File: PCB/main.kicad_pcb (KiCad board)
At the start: 2 copper layers, 135.6 x 65.7 mm, 103 parts, among them K1 HK19F-DCxxV-SHC, Q1 BC337, Q10 BC817, Q11 BC817, Q12 TPCA8120,L1Q, Q13 BC817, Q14 BC817, Q15 BC817, Q16 TPCA8120,L1Q, Q17 BC817, Q18 TPCA8120,L1Q, Q2 BC817, Q3 TPCA8120,L1Q, Q4 BC817, Q5 TPCA8120,L1Q, Q6 TPCA8120,L1Q, Q7 TPCA8120,L1Q, Q8 BC817, Q9 BC817, SW1 config, U1 ESP32-S2-DevKitM, U2 L7805

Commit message: First release for a single (66mm * 118mm) PCB ;-)
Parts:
- removed Q1: BC337, Package_TO_SOT_THT:TO-92_Inline_Wide
- added Q19: BC817, Package_TO_SOT_SMD:SOT-23, F.Cu at (120.2, 68.2)
- Q10, Q11, Q13, Q14, Q15, Q4, Q8, Q9, R11, R12, R3, R4, RA14, RA15, RA16, RA17, RA20, RA22, RA23, RA24, RA25, RA27, RA28, RA30, RA31, RA32, RA33, RA34, RA35, RA36: moved to B.Cu
- RA18, RA19: value 120 -> 33K; moved to B.Cu
- moved SW1 208.7 mm to (129.2, 109.5), turned to -90 degrees
- moved RA3 207.8 mm to (148.9, 103.4)
- moved RA4 207.6 mm to (148.8, 106.0)
- moved RA5 207.5 mm to (148.8, 108.5)
- moved RA7 207.3 mm to (148.9, 94.3)
- moved RA8 207.2 mm to (148.8, 97.5)
- moved RA6 207.2 mm to (148.9, 100.0)
- moved Q4 202.2 mm to (148.2, 70.8), turned to 180 degrees
- moved RV1 197.9 mm to (120.1, 110.6), turned to 90 degrees
- moved R5 197.4 mm to (124.0, 66.7), turned to 90 degrees
- moved R1 195.3 mm to (120.0, 64.5), turned to 180 degrees
- moved RV2 192.2 mm to (114.5, 115.7), turned to -90 degrees
- moved R2 191.8 mm to (116.2, 68.7), turned to -90 degrees
- moved RA14 185.8 mm to (132.6, 80.1), turned to 90 degrees
- moved RA16 185.7 mm to (133.0, 94.4), turned to -90 degrees
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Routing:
- net GND: track 0.00 -> 461.9 mm, vias 0 -> 9
- net +12V: track 0.00 -> 233.5 mm, vias 0 -> 8
- net tempPower: track 0.00 -> 185.0 mm, vias 0 -> 2
- net 5V: track 0.00 -> 169.7 mm, vias 0 -> 5
- net c_rearLight: track 0.00 -> 145.7 mm, vias 0 -> 1
- net i_bykeStand: track 0.00 -> 128.3 mm, vias 0 -> 1
- net Net-(D1-A): track 0.00 -> 85.9 mm, vias 0 -> 1
- net i_startButton: track 0.00 -> 85.8 mm, vias 0 -> 1
- net Net-(Q10-C): track 0.00 -> 84.5 mm, vias 0 -> 3
- net Net-(Q6-G): track 0.00 -> 84.1 mm, vias 0 -> 1
- net Net-(Q12-G): track 0.00 -> 83.6 mm, vias 0 -> 3
- net c_rightArrow: track 0.00 -> 80.9 mm, vias 0 -> 3
- net i_upLight: track 0.00 -> 71.4 mm
- net c_engineOFF: track 0.00 -> 71.3 mm, vias 0 -> 1
- net i_downLight: track 0.00 -> 67.9 mm
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- added copper zone on B.Cu, net GND
- added copper zone on F.Cu, net GND
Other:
- board size 135.6 x 65.7 mm -> 117.9 x 65.7 mm

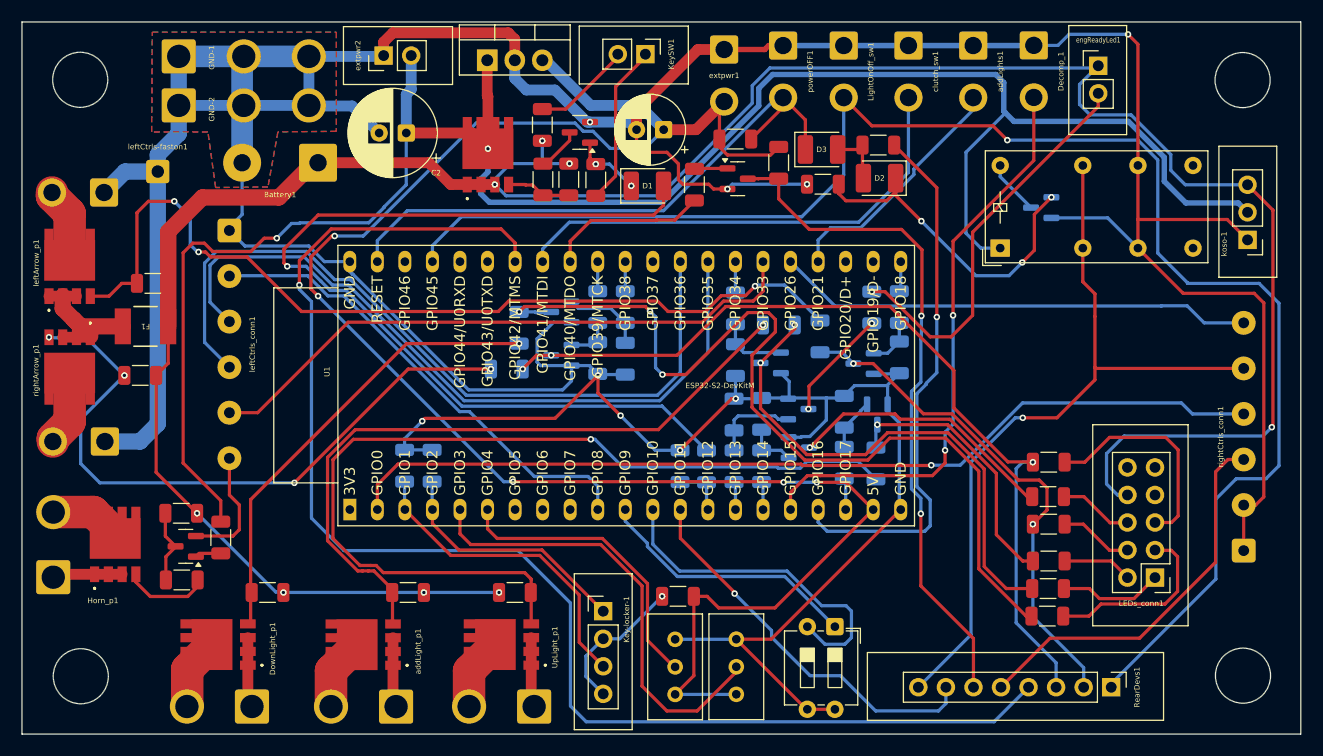
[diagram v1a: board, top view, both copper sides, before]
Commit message: Fixes and size reductuion
- Mosfets' power lines have been added
- 1.5 mm size reduction
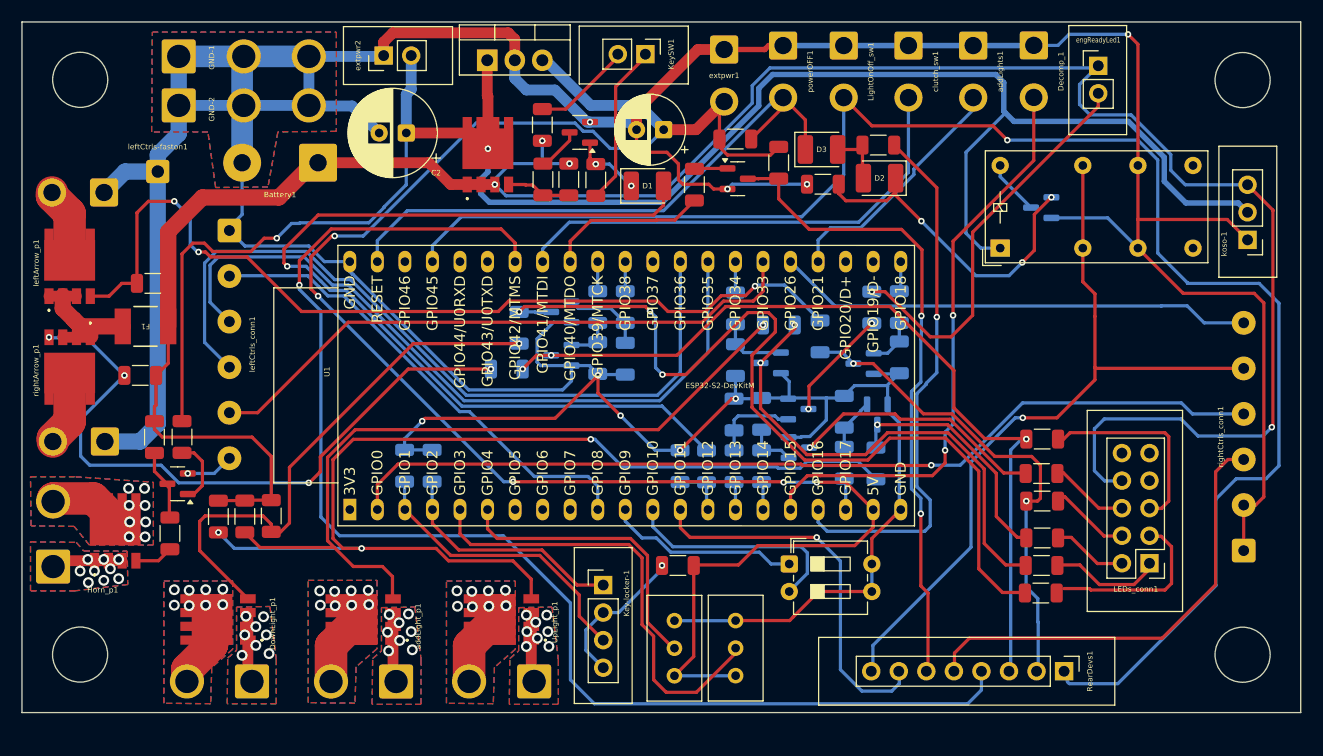
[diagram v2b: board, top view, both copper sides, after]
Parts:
- moved RA10 28.2 mm to (72.3, 99.3), turned to -90 degrees
- moved RA9 16.6 mm to (74.8, 99.3), turned to -90 degrees
- moved RA29 9.93 mm to (69.0, 92.0)
- moved RA21 7.44 mm to (66.4, 92.0), turned to 90 degrees
- moved SW1 7.15 mm to (125.0, 103.7), turned to 0 degrees
- moved RA11 7.06 mm to (77.2, 99.3), turned to -90 degrees
- moved Q17 5.82 mm to (68.6, 96.3)
- moved RearDevs1 4.59 mm to (150.3, 113.6)
- moved RA26 4.43 mm to (67.9, 100.9), turned to 90 degrees
- moved R6 2.84 mm to (114.7, 103.8)
- moved Key-locker-1 2.41 mm to (107.8, 105.6)
- moved DownLight_p1 2.31 mm to (75.4, 114.5)
- moved Q5 2.31 mm to (85.7, 108.8)
- moved Q6 2.31 mm to (98.4, 108.8)
- moved Q7 2.31 mm to (72.3, 108.8)
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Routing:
- net +12V: track 233.5 -> 217.8 mm, vias 8 -> 4
- net Net-(Q6-G): track 84.1 -> 95.6 mm, vias 1 -> 3
- net tempPower: track 185.0 -> 174.4 mm
- net Net-(U1-GPIO10/TOUCH10/ADC1_CH9/FSPICS0/FSPIIO4): track 31.5 -> 21.1 mm
- net GND: track 461.9 -> 452.3 mm
- net Net-(Q7-G): track 42.3 -> 49.9 mm
- net Net-(Q5-G): track 63.9 -> 71.2 mm
- net c_horn: track 11.2 -> 4.42 mm, vias 0 -> 1
- net Net-(U1-GPIO9/TOUCH9/ADC1_CH8/FSPIHD): track 24.6 -> 17.8 mm
- net i_bykeStand: track 128.3 -> 122.3 mm
- net c_brakeSwitch: track 36.0 -> 41.9 mm
- net c_rearLight: track 145.7 -> 150.9 mm
- net Net-(Q18-G): track 7.95 -> 3.57 mm
- net Net-(Q17-B): track 2.41 -> 6.11 mm
- net c_startEngine: track 63.0 -> 59.8 mm
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- added copper zone on B.Cu, net Net-(DownLight_p1-Pin_1)
- added copper zone on F.Cu, net Net-(DownLight_p1-Pin_1)
- added copper zone on B.Cu, net Net-(DownLight_p1-Pin_2)
- added copper zone on F.Cu, net Net-(DownLight_p1-Pin_2)
- added copper zone on B.Cu, net Net-(Horn_p1-Pin_1)
- added copper zone on F.Cu, net Net-(Horn_p1-Pin_1)
- added copper zone on B.Cu, net Net-(Horn_p1-Pin_2)
- added copper zone on F.Cu, net Net-(Horn_p1-Pin_2)
- added copper zone on B.Cu, net Net-(Q5-D_1)
- added copper zone on F.Cu, net Net-(Q5-D_1)
- added copper zone on B.Cu, net Net-(Q5-S_1)
- added copper zone on F.Cu, net Net-(Q5-S_1)
- added copper zone on B.Cu, net Net-(Q6-D_1)
- added copper zone on F.Cu, net Net-(Q6-D_1)
- added copper zone on B.Cu, net Net-(Q6-S_1)
- added copper zone on F.Cu, net Net-(Q6-S_1)
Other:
- board size 117.9 x 65.7 mm -> 117.9 x 63.7 mm

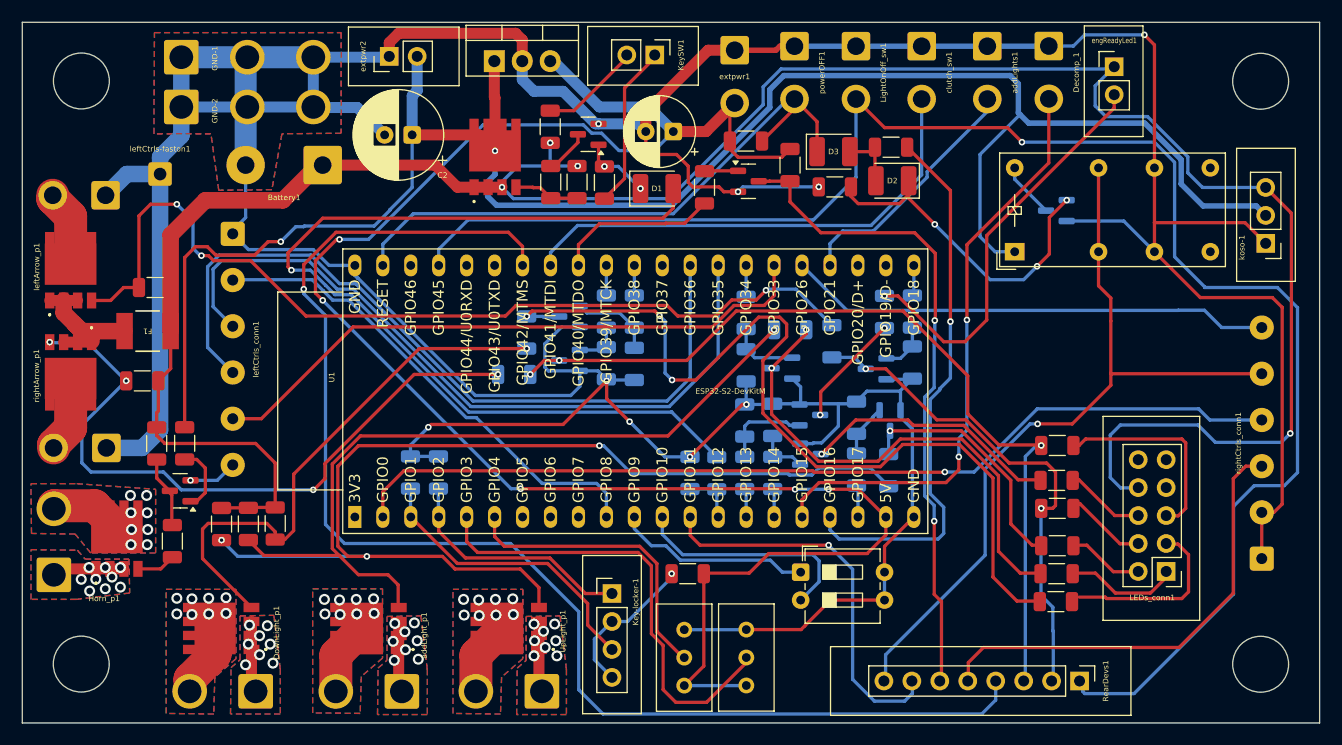
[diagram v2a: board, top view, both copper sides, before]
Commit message: Updates and size reduction
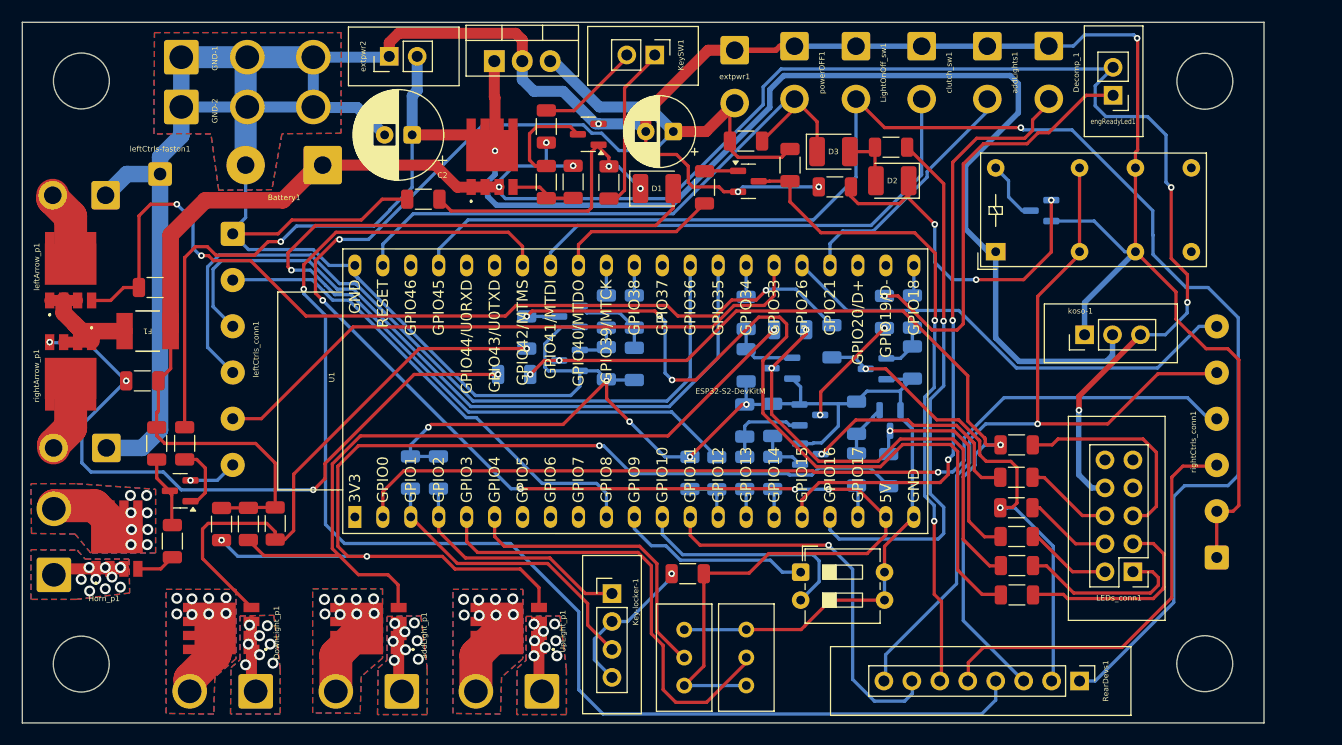
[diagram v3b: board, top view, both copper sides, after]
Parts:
- added R13: 100K, Resistor_SMD:R_1206_3216Metric, F.Cu at (90.7, 69.8)
- moved koso-1 18.4 mm to (150.8, 82.1), turned to 90 degrees
- moved rightCtrls_conn1 4.09 mm to (162.8, 102.4)
- moved RA3 3.79 mm to (144.6, 100.5)
- moved RA6 3.72 mm to (144.6, 97.8)
- moved RA7 3.70 mm to (144.6, 92.1)
- moved RA4 3.68 mm to (144.6, 103.1)
- moved RA8 3.67 mm to (144.6, 95.1)
- moved RA5 3.60 mm to (144.6, 105.8)
- moved LEDs_conn1 3.02 mm to (155.2, 103.7)
- moved engReadyLed1 2.60 mm to (153.4, 60.4), turned to 180 degrees
- moved K1 1.73 mm to (142.7, 74.6)
- moved Q4 1.40 mm to (146.8, 70.8)
- moved R8 0.41 mm to (107.5, 68.3)
- moved R10 0.41 mm to (101.9, 68.2)
- moved R7 0.36 mm to (101.9, 63.2)
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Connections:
- RA14 pad 2: Net-(engReadyLed1-Pin_2) -> Net-(engReadyLed1-Pin_1)
- engReadyLed1 pad 1: +12V -> Net-(engReadyLed1-Pin_1)
- engReadyLed1 pad 2: Net-(engReadyLed1-Pin_2) -> +12V
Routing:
- net Net-(engReadyLed1-Pin_1): track 0.00 -> 39.4 mm, vias 0 -> 1
- net Net-(engReadyLed1-Pin_2): track 37.1 -> 0.00 mm, vias 1 -> 0
- net +12V: track 217.8 -> 197.7 mm, vias 4 -> 6
- net Net-(D1-K): track 6.30 -> 26.4 mm
- net c_rearLight: track 150.9 -> 136.7 mm
- net GND: track 452.3 -> 463.8 mm
- net tempPower: track 174.4 -> 168.1 mm
- net Net-(LEDs_conn1-Pin_1): track 10.4 -> 15.9 mm
- net Net-(Q2-C): track 4.10 -> 9.25 mm
- net c_brakeSwitch: track 41.9 -> 38.1 mm
- net c_engineOFF: track 71.6 -> 75.0 mm
- net Net-(Q8-C): track 45.1 -> 42.0 mm
- net Net-(Q10-C): track 83.0 -> 80.3 mm
- net Net-(LEDs_conn1-Pin_3): track 16.1 -> 18.8 mm
- net Net-(Q9-C): track 22.6 -> 20.2 mm
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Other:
- board size 117.9 x 63.7 mm -> 112.9 x 63.7 mm

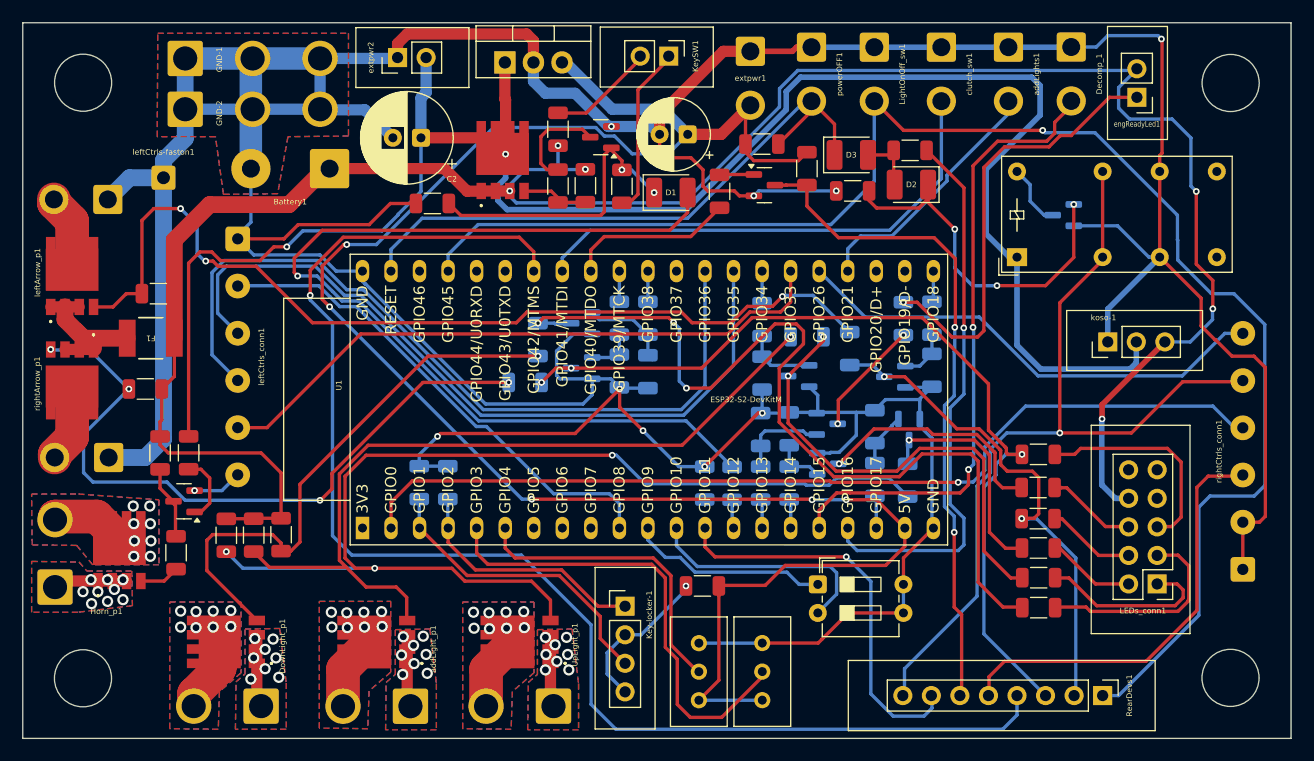
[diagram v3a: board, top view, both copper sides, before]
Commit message: Connectors changing
In order to reuse the already used cables, all the input signal connectors have been changed from solder-wires-sockets to pin-header connectors.
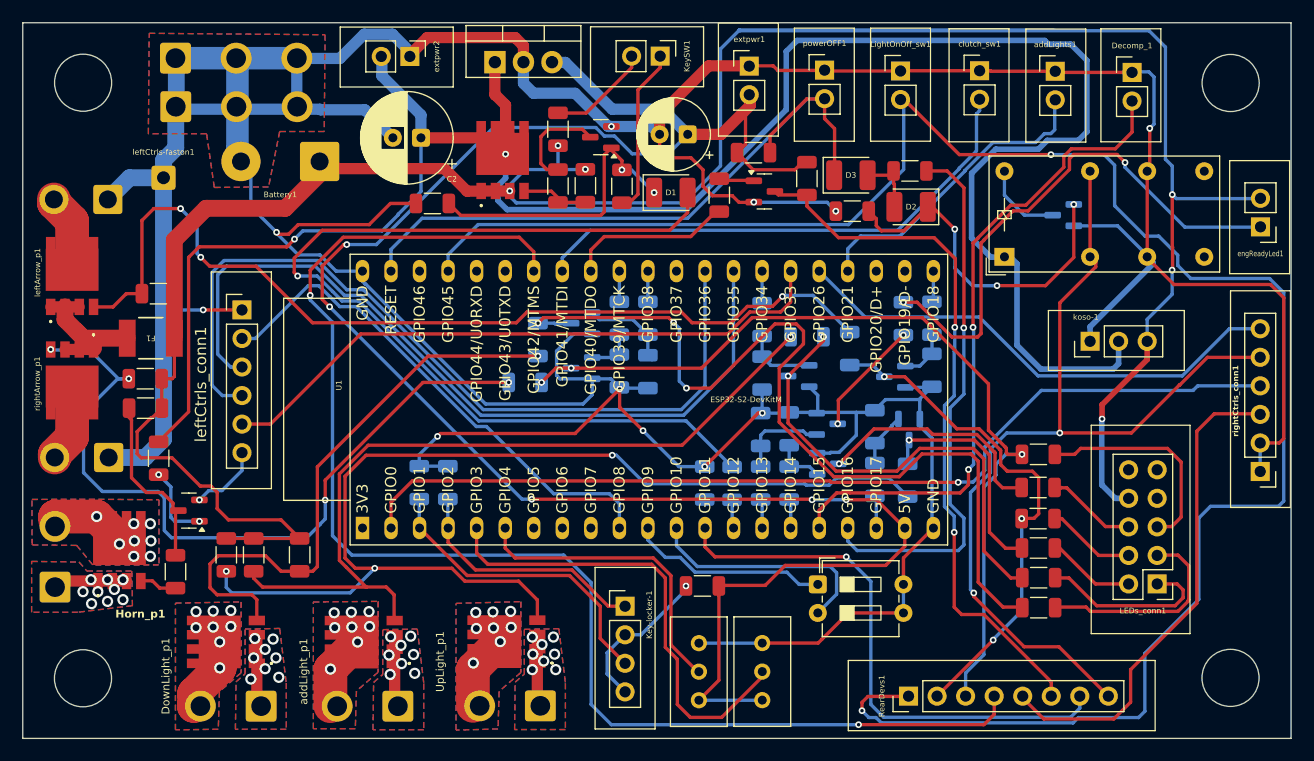
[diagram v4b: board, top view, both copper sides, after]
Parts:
- Decomp_1, LightOnOff_sw1, addLights1, clutch_sw1, extpwr1, powerOFF1: footprint Connector_Wire:SolderWire-0.75sqmm_1x02_P4.8mm_D1.25mm_OD2.3mm -> Connector_PinHeader_2.54mm:PinHeader_1x02_P2.54mm_Vertical
- DownLight_p1, Horn_p1, UpLight_p1, addLight_p1: footprint Connector_Wire:SolderWire-1.5sqmm_1x02_P6mm_D1.7mm_OD3mm -> Connector_Wire:SolderWire-1sqmm_1x02_P5.4mm_D1.4mm_OD2.7mm
- GND-1, GND-2: footprint Connector_Wire:SolderWire-1.5sqmm_1x03_P6mm_D1.7mm_OD3mm -> Connector_Wire:SolderWire-1sqmm_1x03_P5.4mm_D1.4mm_OD2.7mm
- leftCtrls_conn1, rightCtrls_conn1: footprint Custom_conn_wire:SolderWire-0.25sqmm_1x06_P4.2mm_D1.0mm_OD2.2mm -> Connector_PinHeader_2.54mm:PinHeader_1x06_P2.54mm_Vertical
- moved RearDevs1 17.3 mm to (133.0, 113.6), turned to 90 degrees
- moved engReadyLed1 15.9 mm to (164.4, 71.9)
- moved rightCtrls_conn1 8.85 mm to (164.3, 93.6), turned to 180 degrees
- moved leftCtrls_conn1 6.34 mm to (73.7, 79.3), turned to 0 degrees
- moved Decomp_1 5.86 mm to (152.9, 58.1), turned to 0 degrees
- moved addLights1 4.68 mm to (146.1, 58.0), turned to 0 degrees
- moved RA21 4.19 mm to (65.2, 88.0), turned to 0 degrees
- moved clutch_sw1 3.99 mm to (139.4, 58.0), turned to 0 degrees
- moved LightOnOff_sw1 3.15 mm to (132.3, 58.0), turned to 0 degrees
- moved RA29 2.71 mm to (66.3, 92.5)
- moved RA11 2.44 mm to (78.9, 101.1)
- moved powerOFF1 2.35 mm to (125.6, 57.9), turned to 0 degrees
- moved D2 1.98 mm to (133.3, 70.1)
- moved RA2 1.83 mm to (133.2, 66.9)
- moved D3 1.80 mm to (127.9, 67.3)
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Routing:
- net +12V: track 197.7 -> 245.3 mm
- net c_rearLight: track 136.7 -> 172.0 mm, vias 1 -> 2
- net tempPower: track 168.1 -> 187.0 mm
- net i_neutral: track 35.4 -> 49.1 mm
- net Net-(Q17-C): track 6.86 -> 16.1 mm
- net Net-(engReadyLed1-Pin_1): track 39.4 -> 48.2 mm, vias 1 -> 2
- net c_engineOFF: track 75.0 -> 81.8 mm, vias 1 -> 2
- net Net-(Q16-G): track 61.5 -> 68.3 mm
- net c_brakeSwitch: track 38.1 -> 44.0 mm
- net i_powerOFF: track 55.5 -> 61.0 mm
- net GND: track 463.8 -> 458.3 mm, vias 9 -> 11
- net i_addLight: track 22.7 -> 27.5 mm
- net c_startEngine: track 59.8 -> 63.6 mm
- net i_downLight: track 67.9 -> 71.6 mm
- net i_decompr: track 56.4 -> 59.1 mm
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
